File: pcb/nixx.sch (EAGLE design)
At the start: 44 parts, among them IC1 24C64ST

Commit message: added bake control
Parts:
- removed C4: 100nF, joyAnalog:CAP0805
- removed IC1: 24C64ST, joyAnalog:24C64ST
- removed R20: 4K7, joyAnalog:RESISTOR0805-RES
- removed R21: 10K, joyAnalog:RESISTOR0805-RES
- added Q13: (no value), nixx:BF820
- added R22, R23: 10K, joyAnalog:RESISTOR0805-RES
- added R24: 4K7, joyAnalog:RESISTOR0805-RES
- added T1: (no value), zetex:PNPSOT323
- added TP2, TP3, TP4: PTR1TP13R, testpad:PTR1TP13R
- R13: value 10K -> 68K
- R19: value 4K7 -> 10K
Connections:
- removed net N$17: TP1.TP, U$2.PA12
- removed net N$18: IC1.SCL, R19.1, U$2.PF1/OSC_OUT
- new net BAKE: R24.2, U$2.PA12
- new net N$19: JP1.1, R13.2, R19.1, T1.E
- new net N$20: R22.1, T1.B
- new net N$22: Q13.C, R19.2, R22.2
- new net N$23: Q13.B, R24.1
- new net N$24: R23.2, T1.C
- net +180V: now also R23.1
- net +3V3: now also JP1.7; no longer C4.1, IC1.VCC, JP1.3, R19.2, R20.2
- net GND: now also Q13.E; no longer C4.2, IC1.A0, IC1.A1, IC1.A2, IC1.GND, IC1.WP, JP1.7, R21.1
- net N$16: now also TP2.TP, U$2.PF1/OSC_OUT; no longer IC1.SDA, R20.1, U$2.PF0/OSC_IN
- net N$2: now also TP1.TP, U$2.PF0/OSC_IN; no longer JP1.1, R13.2
- net STM_DOT_RIGHT: no longer R21.2
- net UART_RX: now also TP4.TP; no longer JP1.4
- net UART_TX: now also TP3.TP; no longer JP1.5
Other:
- note removed: "OPTIONAL"
- moved on the sheet: R13, R19, TP1

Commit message: fixed bake
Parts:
- R15: value 470 -> 1K
- R16: value 0 -> 470
- R19, R22: value 10K -> 100K
- R23: value 10K -> 75K
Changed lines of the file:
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@@
 <part name="+3V4" library="joyAnalog" deviceset="+3V3" device=""/>
 <part name="R14" library="joyAnalog" deviceset="RESISTOR" device="0805-RES" value="470"/>
-<part name="R15" library="joyAnalog" deviceset="RESISTOR" device="0805-RES" value="470"/>
-<part name="R16" library="joyAnalog" deviceset="RESISTOR" device="0805-RES" value="0"/>
+<part name="R15" library="joyAnalog" deviceset="RESISTOR" device="0805-RES" value="1K"/>
+<part name="R16" library="joyAnalog" deviceset="RESISTOR" device="0805-RES" value="470"/>
 <part name="R17" library="joyAnalog" deviceset="RESISTOR" device="0805-RES" value="4K7"/>
 <part name="R18" library="joyAnalog" deviceset="RESISTOR" device="0805-RES" value="4K7"/>
@@
 <part name="+3V6" library="joyAnalog" deviceset="+3V3" device=""/>
 <part name="TP1" library="testpad" deviceset="PTR1" device="TP13R" value="PTR1TP13R"/>
-<part name="R22" library="joyAnalog" deviceset="RESISTOR" device="0805-RES" value="10K"/>
-<part name="R23" library="joyAnalog" deviceset="RESISTOR" device="0805-RES" value="10K"/>
+<part name="R22" library="joyAnalog" deviceset="RESISTOR" device="0805-RES" value="100K"/>
+<part name="R23" library="joyAnalog" deviceset="RESISTOR" device="0805-RES" value="75K"/>
 <part name="T1" library="zetex" deviceset="PNPSOT323" device=""/>
 <part name="Q13" library="nixx" deviceset="BF820" device=""/>
 <part name="R24" library="joyAnalog" deviceset="RESISTOR" device="0805-RES" value="4K7"/>
 <part name="GND18" library="joyAnalog" deviceset="GND" device=""/>
-<part name="R19" library="joyAnalog" deviceset="RESISTOR" device="0805-RES" value="10K"/>
+<part name="R19" library="joyAnalog" deviceset="RESISTOR" device="0805-RES" value="100K"/>
 <part name="TP2" library="testpad" deviceset="PTR1" device="TP13R" value="PTR1TP13R"/>
 <part name="TP3" library="testpad" deviceset="PTR1" device="TP13R" value="PTR1TP13R"/>

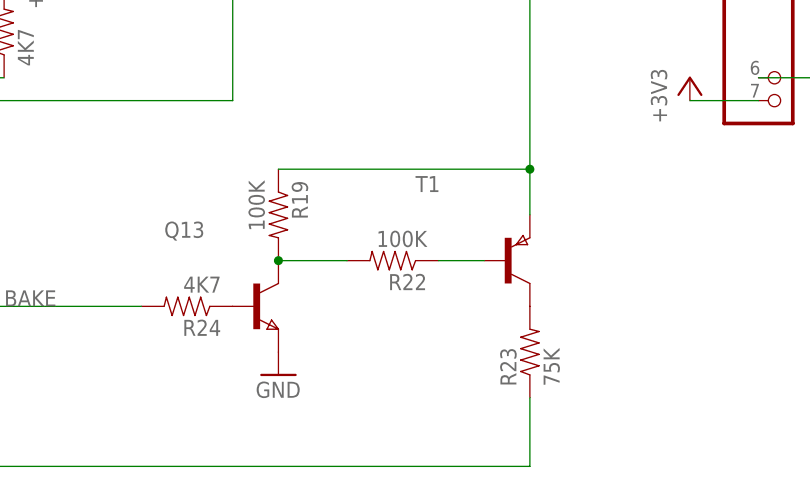
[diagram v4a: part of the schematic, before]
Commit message: 6 tube time display
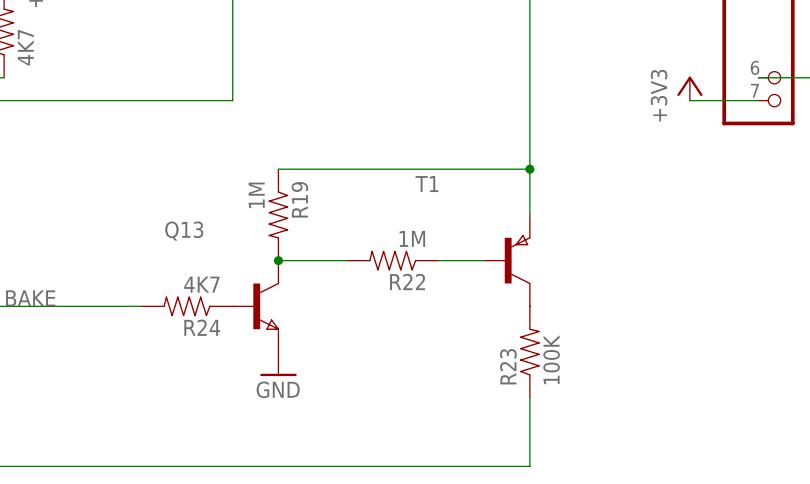
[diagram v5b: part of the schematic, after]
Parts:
- R19, R22: value 100K -> 1M
- R23: value 75K -> 100K
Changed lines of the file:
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@@
 <part name="+3V6" library="joyAnalog" deviceset="+3V3" device=""/>
 <part name="TP1" library="testpad" deviceset="PTR1" device="TP13R" value="PTR1TP13R"/>
-<part name="R22" library="joyAnalog" deviceset="RESISTOR" device="0805-RES" value="100K"/>
-<part name="R23" library="joyAnalog" deviceset="RESISTOR" device="0805-RES" value="75K"/>
+<part name="R22" library="joyAnalog" deviceset="RESISTOR" device="0805-RES" value="1M"/>
+<part name="R23" library="joyAnalog" deviceset="RESISTOR" device="0805-RES" value="100K"/>
 <part name="T1" library="zetex" deviceset="PNPSOT323" device=""/>
 <part name="Q13" library="nixx" deviceset="BF820" device=""/>
 <part name="R24" library="joyAnalog" deviceset="RESISTOR" device="0805-RES" value="4K7"/>
 <part name="GND18" library="joyAnalog" deviceset="GND" device=""/>
-<part name="R19" library="joyAnalog" deviceset="RESISTOR" device="0805-RES" value="100K"/>
+<part name="R19" library="joyAnalog" deviceset="RESISTOR" device="0805-RES" value="1M"/>
 <part name="TP2" library="testpad" deviceset="PTR1" device="TP13R" value="PTR1TP13R"/>
 <part name="TP3" library="testpad" deviceset="PTR1" device="TP13R" value="PTR1TP13R"/>

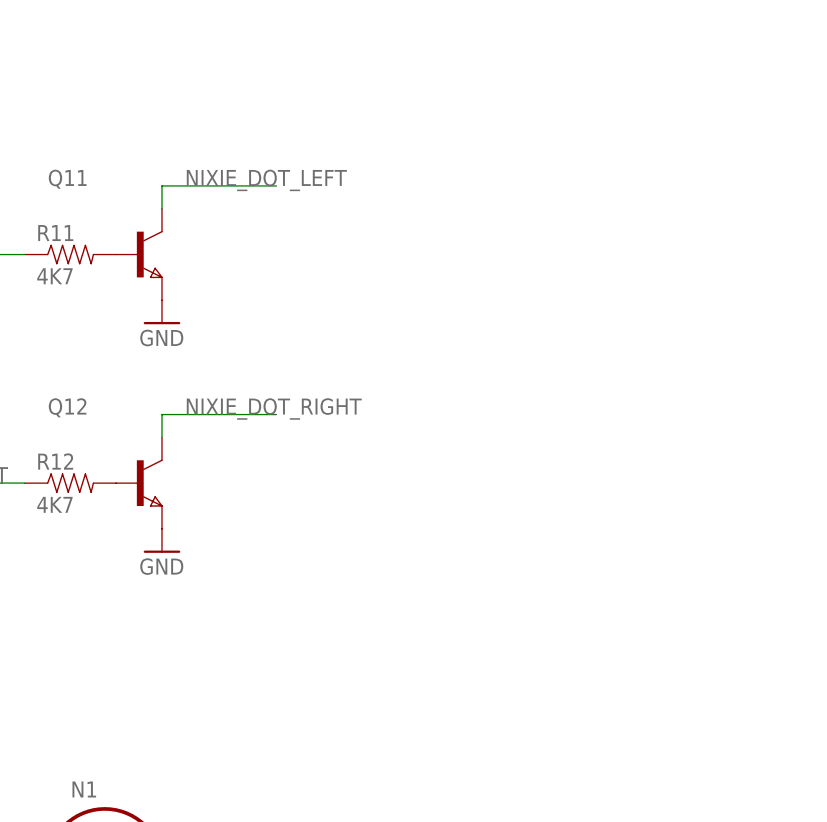
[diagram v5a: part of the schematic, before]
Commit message: added nixie dot current limit resistor
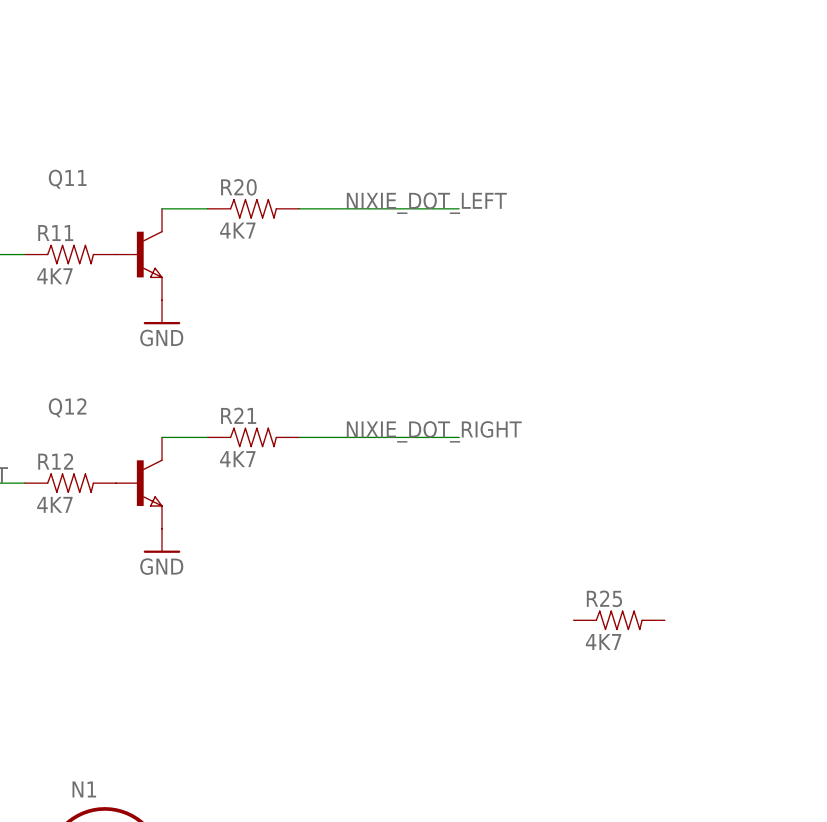
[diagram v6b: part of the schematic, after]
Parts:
- added R20, R21, R25: 4K7, joyAnalog:RESISTOR0805-RES
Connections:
- new net N$17: Q12.C, R21.1
- new net N$18: Q11.C, R20.1
- net NIXIE_DOT_LEFT: now also R20.2; no longer Q11.C
- net NIXIE_DOT_RIGHT: now also R21.2; no longer Q12.C
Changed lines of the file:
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@@
 <?xml version="1.0" encoding="utf-8"?>
 <!DOCTYPE eagle SYSTEM "eagle.dtd">
-<eagle version="8.2.0">
+<eagle version="8.2.2">
 <drawing>
 <settings>
@@
 <part name="TP3" library="testpad" deviceset="PTR1" device="TP13R" value="PTR1TP13R"/>
 <part name="TP4" library="testpad" deviceset="PTR1" device="TP13R" value="PTR1TP13R"/>
+<part name="R20" library="joyAnalog" deviceset="RESISTOR" device="0805-RES" value="4K7"/>
+<part name="R21" library="joyAnalog" deviceset="RESISTOR" device="0805-RES" value="4K7"/>
+<part name="R25" library="joyAnalog" deviceset="RESISTOR" device="0805-RES" value="4K7"/>
 </parts>
 <sheets>
@@
 <instance part="TP3" gate="G$1" x="441.96" y="43.18" rot="R90"/>
 <instance part="TP4" gate="G$1" x="441.96" y="40.64" rot="R90"/>
+<instance part="R20" gate="G$1" x="238.76" y="53.34"/>
+<instance part="R21" gate="G$1" x="238.76" y="27.94"/>
+<instance part="R25" gate="G$1" x="279.4" y="7.62"/>
 </instances>
 <busses>
@@
 </segment>
 <segment>
-<pinref part="Q11" gate="A" pin="C"/>
-<wire x1="228.6" y1="53.34" x2="228.6" y2="55.88" width="0.1524" layer="91"/>
-<wire x1="228.6" y1="55.88" x2="241.3" y2="55.88" width="0.1524" layer="91"/>
-<label x="231.14" y="55.88" size="1.778" layer="95"/>
+<pinref part="R20" gate="G$1" pin="2"/>
+<wire x1="261.62" y1="53.34" x2="243.84" y2="53.34" width="0.1524" layer="91"/>
+<label x="248.92" y="53.34" size="1.778" layer="95"/>
 </segment>
 </net>
@@
 </segment>
 <segment>
-<pinref part="Q12" gate="A" pin="C"/>
-<wire x1="228.6" y1="27.94" x2="228.6" y2="30.48" width="0.1524" layer="91"/>
-<wire x1="228.6" y1="30.48" x2="241.3" y2="30.48" width="0.1524" layer="91"/>
-<label x="231.14" y="30.48" size="1.778" layer="95"/>
+<pinref part="R21" gate="G$1" pin="2"/>
+<wire x1="261.62" y1="27.94" x2="243.84" y2="27.94" width="0.1524" layer="91"/>
+<label x="248.92" y="27.94" size="1.778" layer="95"/>
 </segment>
 </net>
@@
 </segment>
 </net>
+<net name="N$17" class="0">
+<segment>
+<pinref part="Q12" gate="A" pin="C"/>
+<pinref part="R21" gate="G$1" pin="1"/>
+<wire x1="228.6" y1="27.94" x2="233.68" y2="27.94" width="0.1524" layer="91"/>
+</segment>
+</net>
+<net name="N$18" class="0">
+<segment>
+<pinref part="Q11" gate="A" pin="C"/>
+<pinref part="R20" gate="G$1" pin="1"/>
+<wire x1="228.6" y1="53.34" x2="233.68" y2="53.34" width="0.1524" layer="91"/>
+</segment>
+</net>

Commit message: main clock board adj
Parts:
- removed R25: 4K7, joyAnalog:RESISTOR0805-RES
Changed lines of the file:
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@@
 <part name="R20" library="joyAnalog" deviceset="RESISTOR" device="0805-RES" value="4K7"/>
 <part name="R21" library="joyAnalog" deviceset="RESISTOR" device="0805-RES" value="4K7"/>
-<part name="R25" library="joyAnalog" deviceset="RESISTOR" device="0805-RES" value="4K7"/>
 </parts>
 <sheets>
@@
 <instance part="R20" gate="G$1" x="238.76" y="53.34"/>
 <instance part="R21" gate="G$1" x="238.76" y="27.94"/>
-<instance part="R25" gate="G$1" x="279.4" y="7.62"/>
 </instances>
 <busses>
